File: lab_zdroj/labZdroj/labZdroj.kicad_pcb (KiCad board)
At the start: 2 copper layers, 36 parts, among them J1 24V st, J2 0-30V ss, T1 BC327, T2 BC547, T3 BC547, U1 LM350_TO220

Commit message: Rozpracovaný pcb.
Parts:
- C2, C5, D10, D5, D6, DZ1, R1, R10, R11, R14, R2, R4, R6, R7, R8, R9: moved to B.Cu
- moved C4 183.7 mm to (100.7, 99.7)
- moved J1 164.6 mm to (100.1, 74.7), turned to 270 degrees
- moved J_D7 163.6 mm to (128.1, 104.4)
- moved D6 154.3 mm to (112.6, 95.4)
- moved D4 153.4 mm to (97.6, 89.9)
- moved R2 152.7 mm to (127.1, 95.5), turned to 180 degrees
- moved C3 151.4 mm to (112.1, 99.7)
- moved R9 135.0 mm to (149.0, 95.5), turned to 180 degrees
- moved D3 116.7 mm to (110.6, 82.1)
- moved J_D9 115.1 mm to (144.6, 104.5)
- moved D8 112.6 mm to (152.4, 75.3), turned to 90 degrees
- moved D1 110.7 mm to (110.3, 64.4), turned to 180 degrees
- moved C2 109.2 mm to (162.2, 70.4), turned to 270 degrees
- moved D5 108.6 mm to (101.1, 95.4)
- moved C5 102.8 mm to (185.2, 98.8), turned to 180 degrees
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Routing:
- net +24V: track 0.00 -> 80.8 mm
- net GND: track 0.00 -> 30.3 mm
- net Net-(C4-Pad1): track 0.00 -> 20.1 mm
- net Net-(D1-Pad2): track 0.00 -> 11.3 mm
- net Net-(D8-Pad2): track 0.00 -> 7.55 mm

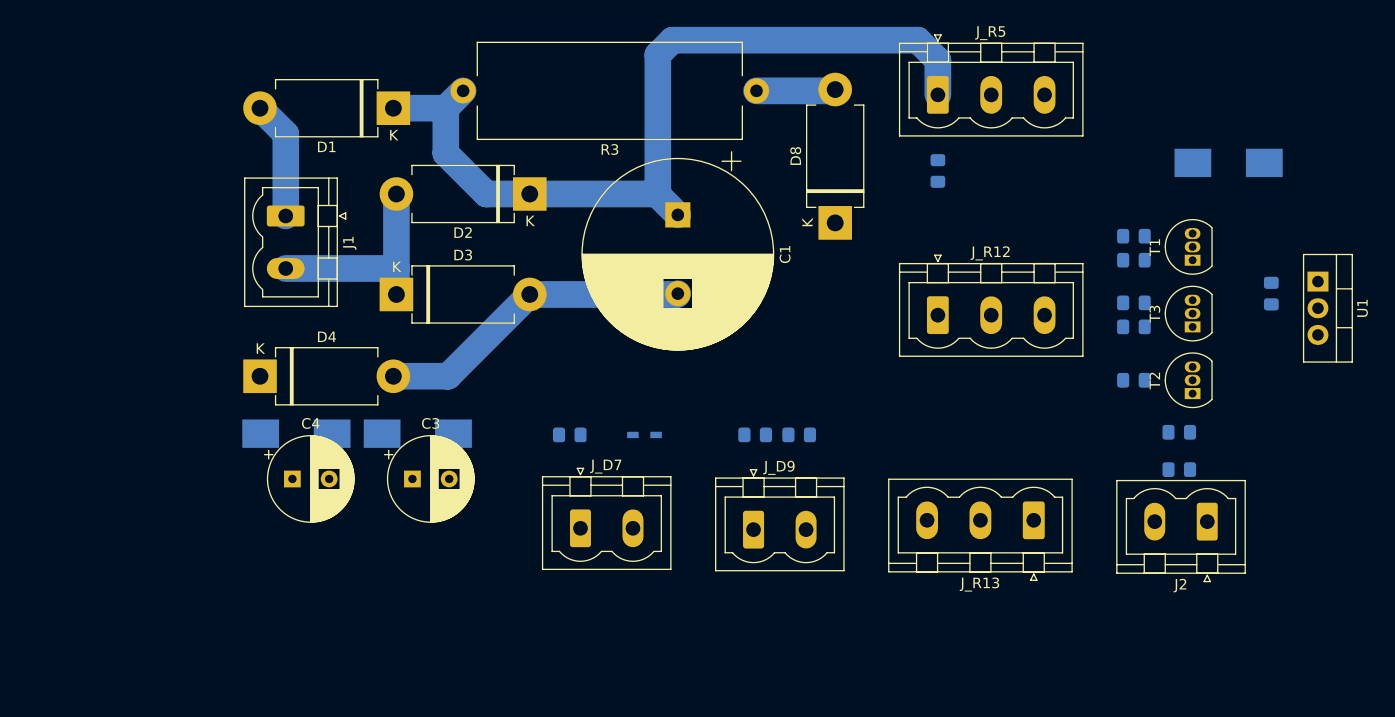
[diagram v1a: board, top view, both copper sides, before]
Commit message: pcb bez gnd plochy a všechny tři tranzistory jsou v smd provedení
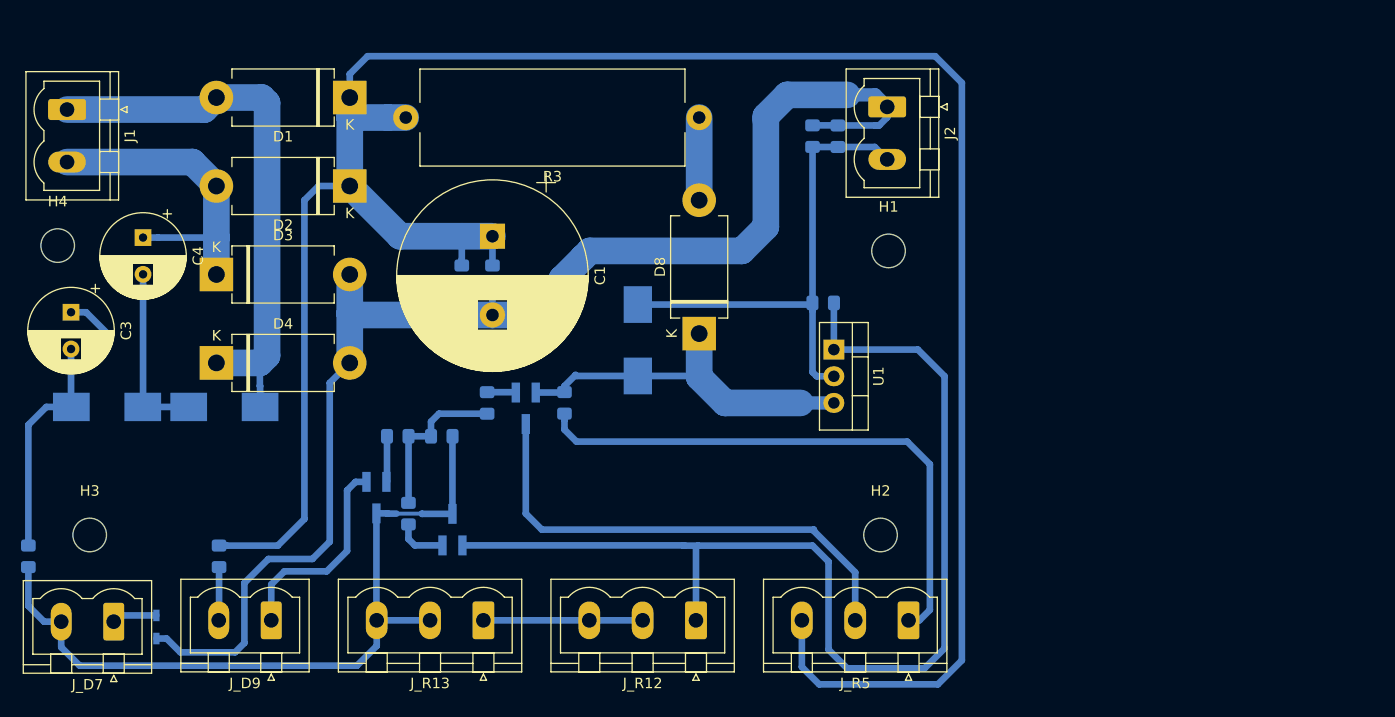
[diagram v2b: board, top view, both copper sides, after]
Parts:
- added H1: MountingHole, MountingHole:MountingHole_3.2mm_M3, F.Cu at (157.5, 78.0)
- added H2: MountingHole, MountingHole:MountingHole_3.2mm_M3, F.Cu at (156.7, 105.0)
- added H3: MountingHole, MountingHole:MountingHole_3.2mm_M3, F.Cu at (81.4, 105.0)
- added H4: MountingHole, MountingHole:MountingHole_3.2mm_M3, F.Cu at (78.4, 77.5)
- T1, T2, T3: footprint Package_TO_SOT_THT:TO-92_Inline -> Package_TO_SOT_SMD:SOT-23_Handsoldering; moved to B.Cu
- moved T2 78.4 mm to (108.7, 101.5), turned to 270 degrees
- moved T3 73.1 mm to (116.0, 104.5)
- moved R10 71.3 mm to (111.8, 103.0), turned to 90 degrees
- moved R8 70.3 mm to (110.7, 95.6), turned to 0 degrees
- moved R7 67.1 mm to (114.9, 95.6)
- moved T1 65.0 mm to (122.9, 93.0), turned to 270 degrees
- moved R6 63.1 mm to (119.3, 92.5), turned to 90 degrees
- moved D10 58.7 mm to (133.6, 86.5), turned to 90 degrees
- moved R4 56.5 mm to (126.6, 92.4), turned to 270 degrees
- moved R9 56.4 mm to (93.7, 107.1), turned to 90 degrees
- moved J_R13 53.3 mm to (118.9, 113.2)
- moved R2 52.8 mm to (75.6, 107.1), turned to 90 degrees
- moved J_R5 50.1 mm to (159.4, 113.2), turned to 180 degrees
- moved DZ1 50.0 mm to (87.8, 113.8), turned to 90 degrees
- moved J2 49.9 mm to (157.4, 64.3), turned to 270 degrees
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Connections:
- J2 pad 1: Net-(C5-Pad1) -> GND
- J2 pad 2: GND -> Net-(C5-Pad1)
- J_D7 pad 1: Net-(J_D7-Pad1) -> Net-(DZ1-Pad2)
- J_D7 pad 2: Net-(DZ1-Pad2) -> Net-(J_D7-Pad2)
- J_R13 pad 2: Net-(J_D7-Pad1) -> Net-(J_D7-Pad2)
- J_R13 pad 3: Net-(J_D7-Pad1) -> Net-(J_D7-Pad2)
- J_R5 pad 1: +24V -> Net-(J_R5-Pad1)
- J_R5 pad 3: Net-(J_R5-Pad3) -> +24V
- R2 pad 1: Net-(J_D7-Pad1) -> Net-(J_D7-Pad2)
- R4 pad 2: Net-(J_R5-Pad3) -> Net-(J_R5-Pad1)
- R7 pad 2: Net-(J_D7-Pad1) -> Net-(J_D7-Pad2)
- T2 pad 3: Net-(J_D7-Pad1) -> Net-(J_D7-Pad2)
- T3 pad 3: Net-(J_D7-Pad1) -> Net-(J_D7-Pad2)
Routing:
- net +24V: track 80.8 -> 217.9 mm
- net GND: track 30.3 -> 137.7 mm
- net Net-(J_R12-Pad1): track 0.00 -> 105.8 mm
- net Net-(J_D7-Pad2): track 0.00 -> 73.8 mm
- net Net-(J_R5-Pad1): track 0.00 -> 54.0 mm
- net Net-(C5-Pad1): track 0.00 -> 48.0 mm
- net Net-(J_R5-Pad2): track 0.00 -> 46.9 mm
- net Net-(D1-Pad2): track 11.3 -> 53.3 mm
- net Net-(D10-Pad1): track 0.00 -> 35.2 mm
- net Net-(C3-Pad2): track 0.00 -> 21.8 mm
- net Net-(J_D9-Pad1): track 0.00 -> 19.9 mm
- net Net-(C4-Pad2): track 0.00 -> 17.0 mm
- net Net-(R10-Pad2): track 0.00 -> 15.5 mm
- net Net-(J_R12-Pad2): track 0.00 -> 15.2 mm
- net Net-(C4-Pad1): track 20.1 -> 30.6 mm
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
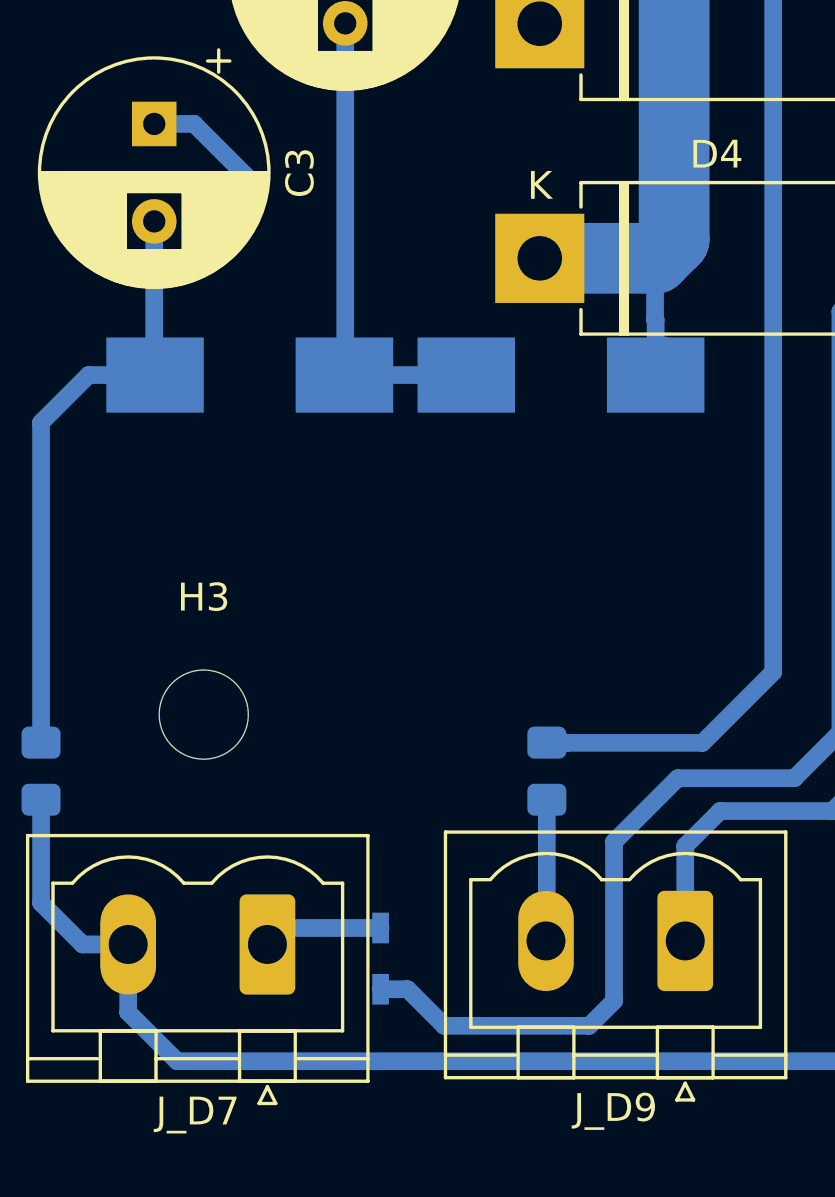
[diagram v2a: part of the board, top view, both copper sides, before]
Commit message: opravena chybějící cesta
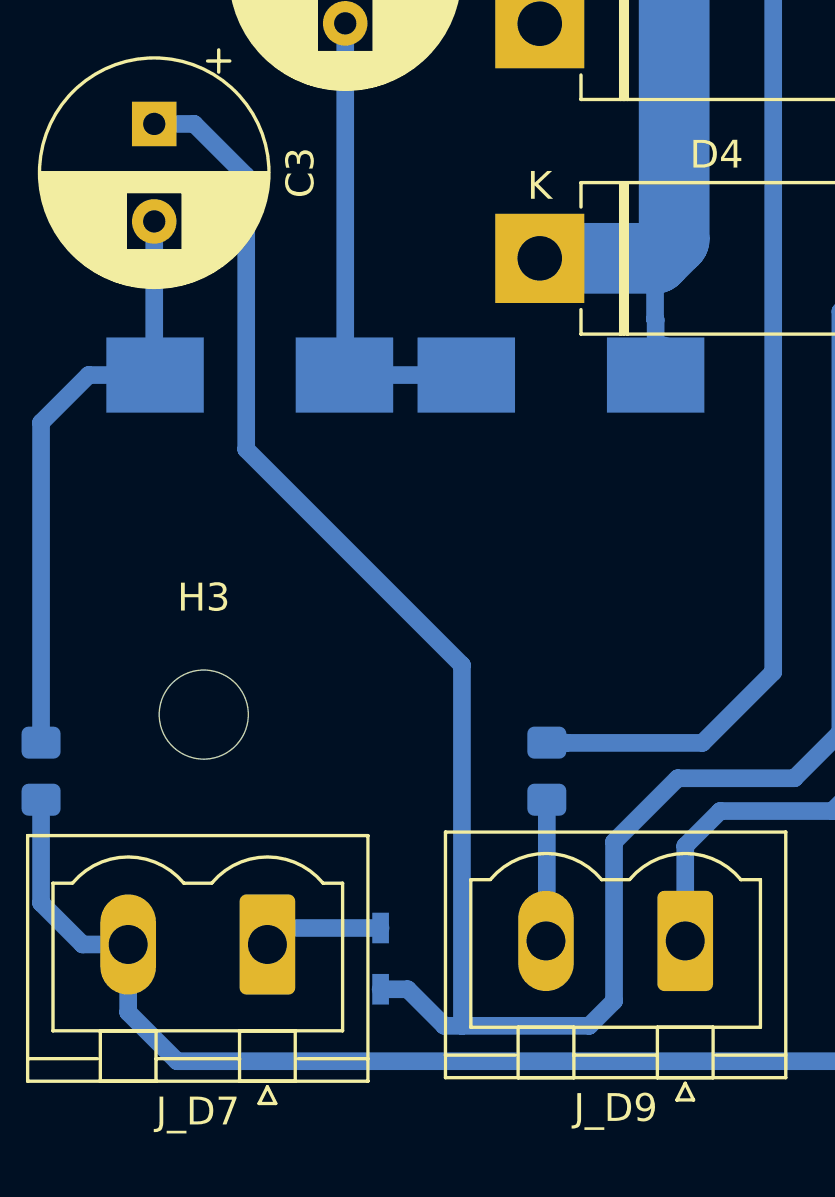
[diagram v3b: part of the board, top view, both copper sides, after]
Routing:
- net GND: track 137.7 -> 171.4 mm
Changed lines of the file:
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@@
     (thickness 1.6)
     (drawings 0)
-    (tracks 195)
+    (tracks 199)
     (zones 0)
     (modules 40)
@@
   (segment (start 119.761 81.416) (end 119.761 84.081) (width 0.635) (layer B.Cu) (net 1))
   (segment (start 104.267 90.551) (end 106.172 88.646) (width 0.635) (layer B.Cu) (net 1))
-  (segment (start 90.043 116.205) (end 95.25 116.205) (width 0.635) (layer B.Cu) (net 1))
   (segment (start 104.267 105.664) (end 104.267 90.551) (width 0.635) (layer B.Cu) (net 1))
   (segment (start 102.616 107.315) (end 104.267 105.664) (width 0.635) (layer B.Cu) (net 1))
@@
   (segment (start 88.73 114.892) (end 87.757 114.892) (width 0.635) (layer B.Cu) (net 1))
   (segment (start 90.043 116.205) (end 88.73 114.892) (width 0.635) (layer B.Cu) (net 1))
+  (segment (start 82.931 85.687) (end 82.931 95.504) (width 0.635) (layer B.Cu) (net 1))
+  (segment (start 82.931 95.504) (end 90.678 103.251) (width 0.635) (layer B.Cu) (net 1))
+  (segment (start 90.678 103.251) (end 90.678 116.205) (width 0.635) (layer B.Cu) (net 1))
+  (segment (start 90.043 116.205) (end 90.678 116.205) (width 0.635) (layer B.Cu) (net 1))
+  (segment (start 90.678 116.205) (end 95.25 116.205) (width 0.635) (layer B.Cu) (net 1))
   (segment (start 111.506 65.278) (end 109.808944 65.278) (width 2.54) (layer B.Cu) (net 2))
   (segment (start 106.172 63.373) (end 106.172 65.278) (width 2.54) (layer B.Cu) (net 2))

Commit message: upgrade pcb, první finální verze.
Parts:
- moved R11 8.69 mm to (156.6, 89.8)
- moved H1 0.51 mm to (157.5, 78.5)
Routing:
- net Net-(C5-Pad1): track 48.0 -> 53.5 mm
- net Net-(D10-Pad1): track 35.2 -> 38.7 mm
- net Net-(J_R12-Pad1): track 105.8 -> 103.8 mm
- added copper zone on B.Cu, net (none)
- added copper zone on B.Cu, net GND
